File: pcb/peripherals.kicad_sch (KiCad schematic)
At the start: 33 parts, among them J102 TO_DISP_INPUT, J103 TO_DISP_OUTPUT, U101 10M02SCE144, Y101 24.000MHz

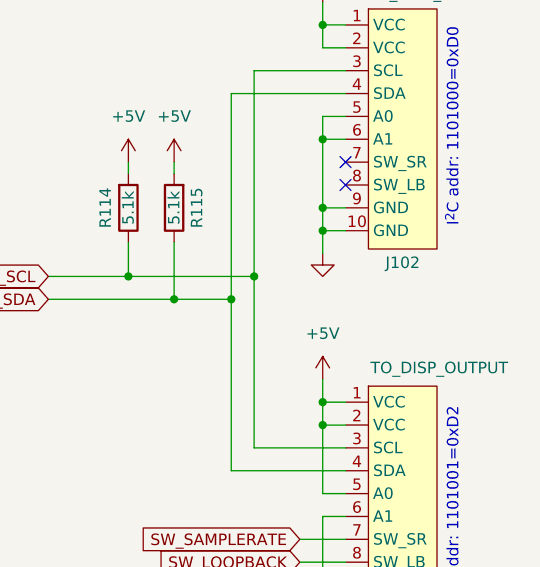
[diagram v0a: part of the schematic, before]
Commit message: Finish assigning footprints to project
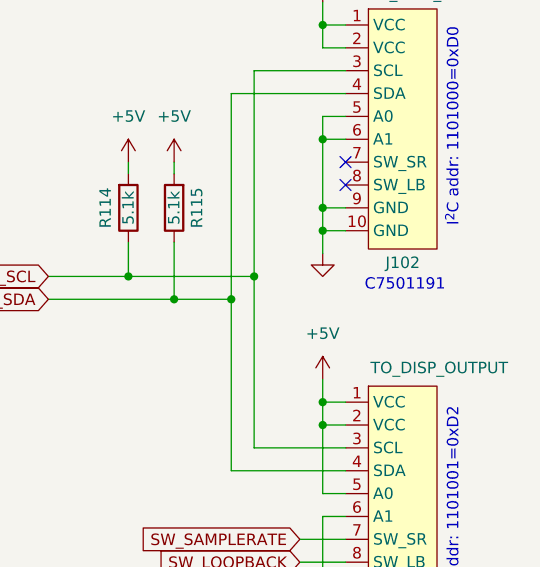
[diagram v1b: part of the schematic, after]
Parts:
- Y101: footprint (none) -> Oscillator:Oscillator_SMD_Abracon_ASE-4Pin_3.2x2.5mm_HandSoldering
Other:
- note added: "C7501191"
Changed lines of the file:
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@@
+		)
+	)
+	(text "C7501191"
+		(exclude_from_sim no)
+		(at 245.364 63.246 0)
+		(effects
+			(font
+				(size 1.27 1.27)
+			)
 		)
 	)
@@
 			)
 		)
-		(property "Footprint" ""
+		(property "Footprint" "Oscillator:Oscillator_SMD_Abracon_ASE-4Pin_3.2x2.5mm_HandSoldering"
 			(at 62.23 156.21 0)
 			(effects

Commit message: Finish drawing IO/Supply board
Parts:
- removed Y101: 24.000MHz, Oscillator:Oscillator_SMD_Abracon_ASE-4Pin_3.2x2.5mm_HandSoldering, symbol Device:Crystal_GND23
- added C150: 1u, Capacitor_SMD:C_0805_2012Metric_Pad1.18x1.45mm_HandSolder, symbol Device:C
- added D108: 3V, Diode_SMD:D_SOD-123, symbol Device:D_Zener
- added R131, R132: 1k, Resistor_SMD:R_0805_2012Metric_Pad1.20x1.40mm_HandSolder, symbol Device:R
- added Y101: 24.000MHz, Oscillator:Oscillator_SMD_Abracon_ASE-4Pin_3.2x2.5mm_HandSoldering, symbol Device:Crystal_GND24
- C142: renamed from C143; value C_{load} -> 15pF
- C143: renamed from C144; value C_{load} -> 15pF
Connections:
- net +3.3V: now also D108.2 (A)
- net +5V: now also R131.1, R132.1; no longer R114.2, R115.2
- net GND: now also C150.2, Y101.2, Y101.4
- net MCU_XTAL1: now also Y101.3
- net MCU_XTAL2: now also Y101.1
- net FPGA_JTAGEN: no longer names the net of R111.2, U101.13 (JTAGEN)
- new net: C150.1, D108.1 (K), R114.2, R115.2, R131.2, R132.2
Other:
- note added: "C16197264"
- note added: "C894641"
- moved on the sheet: C142, C143, R107, R108, R109, R110, R111, R112, R113, R116, TP101, TP102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

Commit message: Add missing CAD models of I/O electronic components
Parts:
- U101: footprint Package_QFP:EQFP-144-1EP_20x20mm_P0.5mm_EP4x4mm_ThermalVias -> adatv2:EQFP-144-1EP_20x20mm_P0.5mm_EP4x4mm
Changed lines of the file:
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@@
 			)
 		)
-		(property "Footprint" "Package_QFP:EQFP-144-1EP_20x20mm_P0.5mm_EP4x4mm_ThermalVias"
+		(property "Footprint" "adatv2:EQFP-144-1EP_20x20mm_P0.5mm_EP4x4mm"
 			(at 47.498 13.208 0)
 			(effects

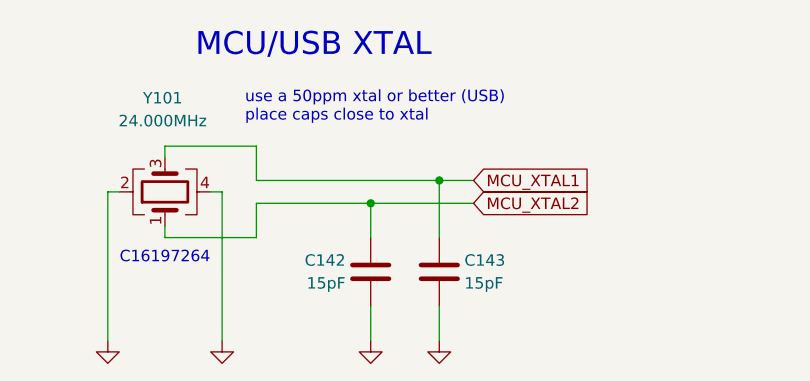
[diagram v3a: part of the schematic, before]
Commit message: Assign FPGA pins, change MCU to STM32F429VET6
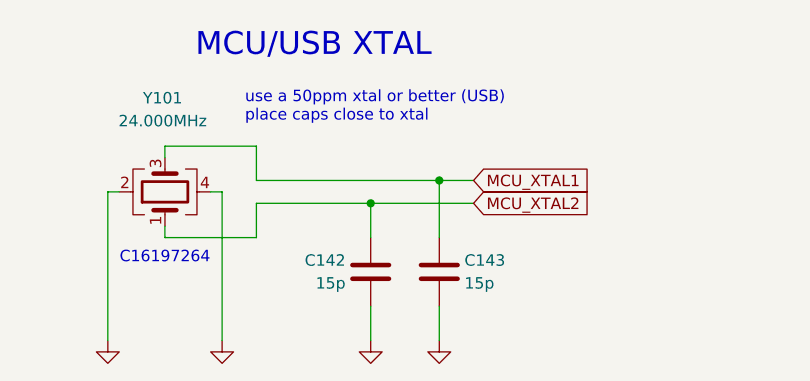
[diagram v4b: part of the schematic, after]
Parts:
- C142, C143: value 15pF -> 15p
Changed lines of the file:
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@@
 			)
 		)
-		(property "Value" "15pF"
+		(property "Value" "15p"
 			(at 81.026 166.37 0)
 			(effects
@@
 			)
 		)
-		(property "Value" "15pF"
+		(property "Value" "15p"
 			(at 94.234 166.37 0)
 			(effects

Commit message: Add PCB production files
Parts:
- TP101, TP102, TP103, TP104, TP105, TP106, TP107, TP108, TP109: footprint TestPoint:TestPoint_Pad_D2.5mm -> TestPoint:TestPoint_Pad_D1.5mm
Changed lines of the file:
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@@
 			)
 		)
-		(property "Footprint" "TestPoint:TestPoint_Pad_D2.5mm"
+		(property "Footprint" "TestPoint:TestPoint_Pad_D1.5mm"
 			(at 62.23 102.87 0)
 			(effects
@@
 			)
 		)
-		(property "Footprint" "TestPoint:TestPoint_Pad_D2.5mm"
+		(property "Footprint" "TestPoint:TestPoint_Pad_D1.5mm"
 			(at 144.78 59.69 0)
 			(effects
@@
 			)
 		)
-		(property "Footprint" "TestPoint:TestPoint_Pad_D2.5mm"
+		(property "Footprint" "TestPoint:TestPoint_Pad_D1.5mm"
 			(at 62.23 110.49 0)
 			(effects
@@
 			)
 		)
-		(property "Footprint" "TestPoint:TestPoint_Pad_D2.5mm"
+		(property "Footprint" "TestPoint:TestPoint_Pad_D1.5mm"
 			(at 62.23 100.33 0)
 			(effects
@@
 			)
 		)
-		(property "Footprint" "TestPoint:TestPoint_Pad_D2.5mm"
+		(property "Footprint" "TestPoint:TestPoint_Pad_D1.5mm"
 			(at 62.23 107.95 0)
 			(effects
@@
 			)
 		)
-		(property "Footprint" "TestPoint:TestPoint_Pad_D2.5mm"
+		(property "Footprint" "TestPoint:TestPoint_Pad_D1.5mm"
 			(at 62.23 97.79 0)
 			(effects
@@
 			)
 		)
-		(property "Footprint" "TestPoint:TestPoint_Pad_D2.5mm"
+		(property "Footprint" "TestPoint:TestPoint_Pad_D1.5mm"
 			(at 62.23 115.57 0)
 			(effects
@@
 			)
 		)
-		(property "Footprint" "TestPoint:TestPoint_Pad_D2.5mm"
+		(property "Footprint" "TestPoint:TestPoint_Pad_D1.5mm"
 			(at 62.23 105.41 0)
 			(effects
@@
 			)
 		)
-		(property "Footprint" "TestPoint:TestPoint_Pad_D2.5mm"
+		(property "Footprint" "TestPoint:TestPoint_Pad_D1.5mm"
 			(at 62.23 113.03 0)
 			(effects
